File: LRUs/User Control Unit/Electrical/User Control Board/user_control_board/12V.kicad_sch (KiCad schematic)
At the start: 7 parts, among them U17 AMS1117-3.3

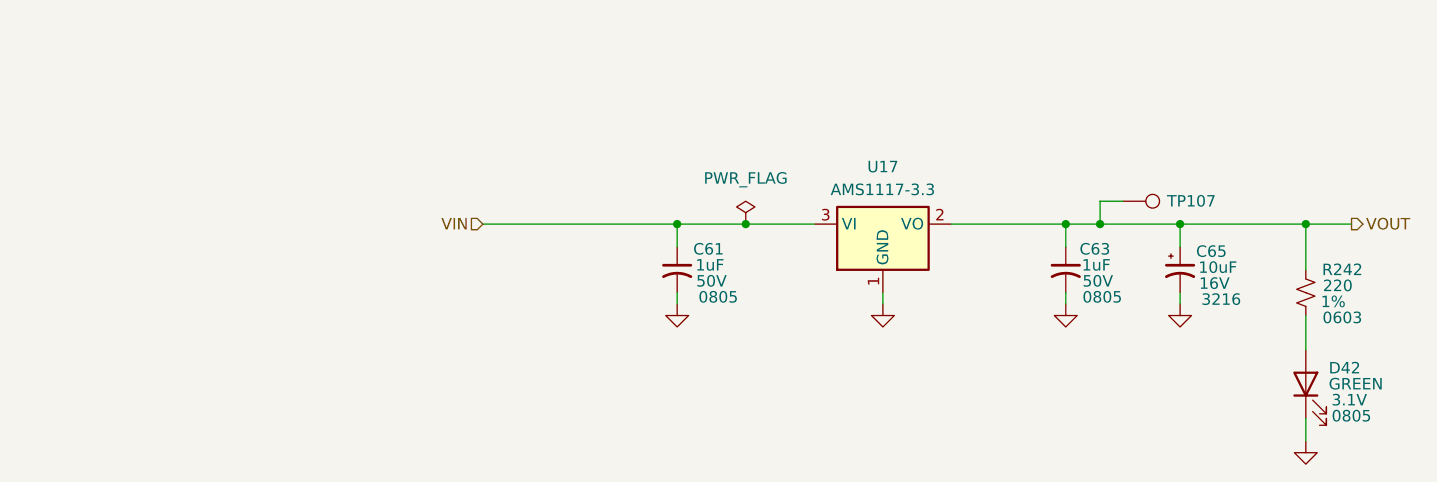
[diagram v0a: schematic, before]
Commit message: Added 12V XL6009 boost converter schematic
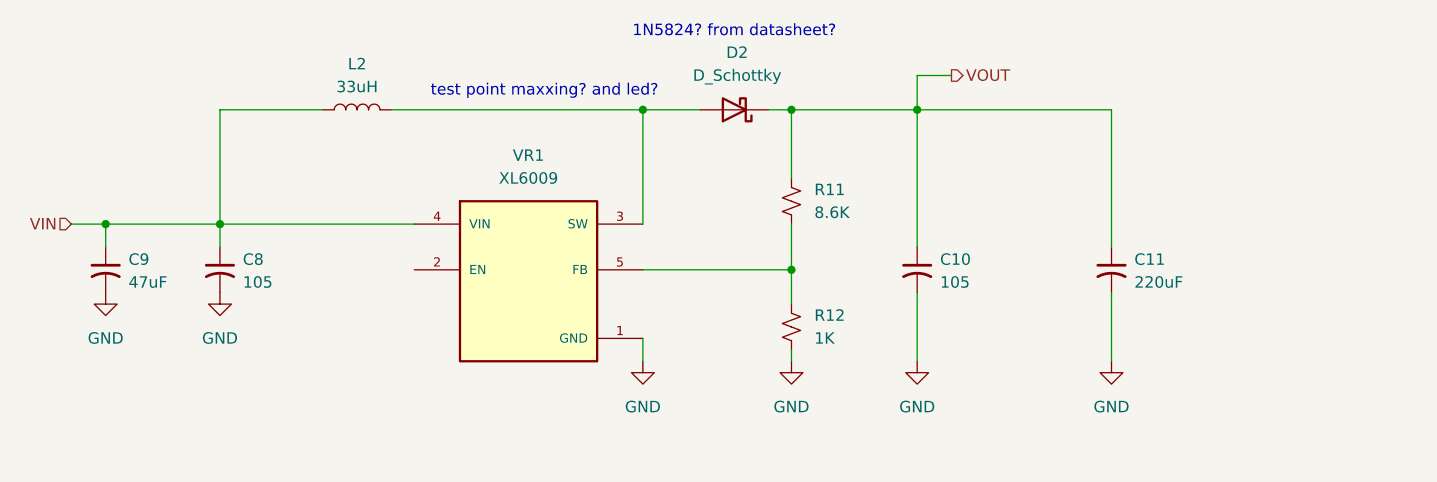
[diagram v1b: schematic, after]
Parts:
- removed C61, C63: 1uF, valve_pcb_footprints:C_0805_2012Metric, symbol Device:C_Small_US
- removed C65: 10uF, Capacitor_Tantalum_SMD:CP_EIA-3216-18_Kemet-A, symbol Device:C_Polarized_Small_US
- removed D42: GREEN, LED_SMD:LED_0805_2012Metric, symbol Device:LED
- removed R242: 220, valve_pcb_footprints:R_0603_1608Metric, symbol Device:R_Small_US
- removed TP107: TestPoint, TestPoint:TestPoint_Pad_D1.0mm, symbol Connector:TestPoint
- removed U17: AMS1117-3.3, Package_TO_SOT_SMD:SOT-223-3_TabPin2, symbol Regulator_Linear:AMS1117-3.3
- added C10: 105, Package_SO:SOIC-8_3.9x4.9mm_P1.27mm, symbol Device:C_Small_US
- added C11: 220uF, Package_SO:SOIC-8_3.9x4.9mm_P1.27mm, symbol Device:C_Small_US
- added C8: 105, XL6009:DPAK170P1435X465-6N, symbol Device:C_Small_US
- added C9: 47uF, symbol Device:C_Small_US
- added D2: D_Schottky, Diode_THT:D_DO-201AD_P15.24mm_Horizontal, symbol Device:D_Schottky
- added L2: 33uH, Relay_THT:Relay_DPDT_Finder_30.22, symbol Device:L
- added R11: 8.6K, symbol Device:R_Small_US
- added R12: 1K, symbol Device:R_Small_US
- added VR1: XL6009, XL6009:DPAK170P1435X465-6N, symbol XL6009:XL6009
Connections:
- net GND: now also C10.2, C11.2, C8.2, C9.2, R12.2, VR1.1 (GND)
- net VIN: now also C8.1, C9.1, L2.1, VR1.4 (VIN)
- net VOUT: now also C10.1, C11.1, D2.1 (K), R11.1
- new net: D2.2 (A), L2.2, VR1.3 (SW), VR1.6 (SW)
- new net: R11.2, R12.1, VR1.5 (FB)
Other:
- note added: "1N5824? from datasheet?"
- note added: "test point maxxing? and led?"

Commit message: footprint and added symbol for audio
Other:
- note added: "COILCRAFT FOR INDUCTOR"
- note added: "texus insturements 12 v boost regulator make schematic from input from 2s battery sends it to another connector *another screw terminal and that connector would send to external module xl6009."
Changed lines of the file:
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@@
+		)
+	)
+	(text "texus insturements 12 v boost regulator\n\nmake schematic from input from 2s battery sends it to another connector *another screw terminal and that connector would send to external module xl6009. "
+		(exclude_from_sim no)
+		(at 108.966 124.714 0)
+		(effects
+			(font
+				(size 1.27 1.27)
+			)
 		)
 	)
@@
 		(effects
 			(font
+				(size 1.27 1.27)
+			)
+		)
+	)
+	(text "COILCRAFT FOR INDUCTOR\n"
+		(exclude_from_sim no)
+		(at 85.852 61.722 0)
+		(effects
+			(font

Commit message: drc run
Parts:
- removed D2: D_Schottky, Diode_THT:D_DO-201AD_P15.24mm_Horizontal, symbol Device:D_Schottky
- removed VR1: XL6009, XL6009:DPAK170P1435X465-6N, symbol XL6009:XL6009
- added C12: 4.7uF, Package_LGA:Bosch_LGA-14_3x2.5mm_P0.5mm, symbol Device:C_Small_US
- added C13: 30pF, Package_LGA:Bosch_LGA-14_3x2.5mm_P0.5mm, symbol Device:C_Small_US
- added C14: 680pF, Package_LGA:Bosch_LGA-14_3x2.5mm_P0.5mm, symbol Device:C_Small_US
- added R10: 1.05M, Package_LGA:Bosch_LGA-14_3x2.5mm_P0.5mm, symbol Device:R_Small_US
- added R13: 32.4k, Package_LGA:Bosch_LGA-14_3x2.5mm_P0.5mm, symbol Device:R_Small_US
- added R14: 127k, Package_LGA:Bosch_LGA-14_3x2.5mm_P0.5mm, symbol Device:R_Small_US
- added TP10, TP6, TP7, TP8, TP9: TestPoint, symbol Connector:TestPoint
- added U1: TPS61089RNRR, RNR0011A, symbol symbols:TPS61089RNRR
- C10: value 105 -> 47uF; footprint Package_SO:SOIC-8_3.9x4.9mm_P1.27mm -> Package_LGA:Bosch_LGA-14_3x2.5mm_P0.5mm
- C11: value 220uF -> 100nF; footprint Package_SO:SOIC-8_3.9x4.9mm_P1.27mm -> Package_LGA:Bosch_LGA-14_3x2.5mm_P0.5mm
- C8: value 105 -> 10uF; footprint XL6009:DPAK170P1435X465-6N -> Package_LGA:Bosch_LGA-14_3x2.5mm_P0.5mm
- C9: value 47uF -> 100nF; footprint (none) -> Package_LGA:Bosch_LGA-14_3x2.5mm_P0.5mm
- L2: value 33uH -> 1.2uH; footprint Relay_THT:Relay_DPDT_Finder_30.22 -> (none)
- R11: value 8.6K -> 118k; footprint (none) -> Package_LGA:Bosch_LGA-14_3x2.5mm_P0.5mm
- R12: value 1K -> 309k; footprint (none) -> Package_LGA:Bosch_LGA-14_3x2.5mm_P0.5mm
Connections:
- net GND: now also R11.2, C12.2, C13.2, C14.2, R14.2, TP10.1, U1.5 (GND); no longer C9.2, R12.2
- net VIN: now also C10.1, C11.1, TP7.1, U1.9 (VIN); no longer C8.1, C9.1
- net VOUT: now also C8.1, R10.1, TP6.1, U1.6 (VOUT); no longer C10.1, C11.1, R11.1
- net at L2.2: now also C9.2, R12.1, TP8.1, U1.11 (SW)
- new net: R12.2, U1.1 (FSW)
- new net: C9.1, U1.10 (BOOT)
- new net: C12.1, U1.2 (VCC), U1.7 (EN)
- new net: R10.2, R11.1, TP9.1, U1.3 (FB)
- new net: C13.1, R13.1, U1.4 (COMP)
- new net: R14.1, U1.8 (ILIM)
- new net: C14.1, R13.2
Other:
- note removed: "1N5824? from datasheet?"
- note removed: "test point maxxing? and led?"
- note removed: "texus insturements 12 v boost regulator make schematic from input from 2s battery sends it to another connector *another screw terminal and that connector would send to external module xl6009."

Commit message: need to run DCR
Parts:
- removed R11: 118k, Package_LGA:Bosch_LGA-14_3x2.5mm_P0.5mm, symbol Device:R_Small_US
- added R16: 18k, valve_pcb_footprints:R_0603_1608Metric, symbol Device:R_Small_US
- added R17: 100k, valve_pcb_footprints:R_0603_1608Metric, symbol Device:R_Small_US
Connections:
- net GND: now also R16.2
- net at R10.2, TP9.1, U1.3 (FB): now also R17.1
- new net: R16.1, R17.2
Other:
- note added: "ILIM = 1030000/RILIM = 8 A"
- note added: "Target FSW = 1.2MHz"
- note added: "Used TI power designer for this."
- note added: "VFB = VOUT * RBOT/(RTOP + RBOT) VOUT = 1.212 (1+ (RTOP/BOT)) VOUT = 1.212 (1+ (1.05*10^6/118*10^3)) = 12"
- note added: "VIN = 7.4 NOMINAL"
- note removed: "COILCRAFT FOR INDUCTOR"
- moved on the sheet: R14, TP10

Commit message: connectors and 5v buck partially done
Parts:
- removed C10: 47uF, Package_LGA:Bosch_LGA-14_3x2.5mm_P0.5mm, symbol Device:C_Small_US
- removed C11, C9: 100nF, Package_LGA:Bosch_LGA-14_3x2.5mm_P0.5mm, symbol Device:C_Small_US
- removed C12: 4.7uF, Package_LGA:Bosch_LGA-14_3x2.5mm_P0.5mm, symbol Device:C_Small_US
- removed C8: 10uF, Package_LGA:Bosch_LGA-14_3x2.5mm_P0.5mm, symbol Device:C_Small_US
- removed R10: 1.05M, Package_LGA:Bosch_LGA-14_3x2.5mm_P0.5mm, symbol Device:R_Small_US
- removed R12: 309k, Package_LGA:Bosch_LGA-14_3x2.5mm_P0.5mm, symbol Device:R_Small_US
- removed R13: 32.4k, Package_LGA:Bosch_LGA-14_3x2.5mm_P0.5mm, symbol Device:R_Small_US
- removed R14: 127k, Package_LGA:Bosch_LGA-14_3x2.5mm_P0.5mm, symbol Device:R_Small_US
- removed U1: TPS61089RNRR, RNR0011A, symbol symbols:TPS61089RNRR
- added C15: 47uF, Capacitor_SMD:C_1206_3216Metric, symbol Device:C_Small_US
- added C16, C20: 100nF, Capacitor_SMD:C_0402_1005Metric, symbol Device:C_Small_US
- added C17: 4.7uF, Capacitor_SMD:C_0805_2012Metric, symbol Device:C_Small_US
- added C18: 30pF, Capacitor_SMD:C_0201_0603Metric, symbol Device:C_Small_US
- added C19: 680pF, Capacitor_SMD:C_0201_0603Metric, symbol Device:C_Small_US
- added C21, C22, C23: 10uF, Capacitor_Tantalum_SMD:CP_EIA-7343-31_Kemet-D, symbol Device:C_Polarized_Small_US
- added R19: 32.4k, Resistor_SMD:R_0603_1608Metric, symbol Device:R_Small_US
- added R20: 127k, Resistor_SMD:R_0603_1608Metric, symbol Device:R_Small_US
- added R21: 309k, Resistor_SMD:R_0603_1608Metric, symbol Device:R_Small_US
- added R22: 1.05M, Resistor_SMD:R_0603_1608Metric, symbol Device:R_Small_US
- added U4: TPS61089RNRR, Package_DFN_QFN:Texas_VQFN-RNR0011A-11, symbol symbols:TPS61089RNRR
- C13: value 30pF -> 47uF; footprint Package_LGA:Bosch_LGA-14_3x2.5mm_P0.5mm -> Capacitor_SMD:C_1206_3216Metric; Footprint_Size (none) -> 1206; JLCPCB Part # (none) -> C76659; Vmax (none) -> 25v
- C14: value 680pF -> 47uF; footprint Package_LGA:Bosch_LGA-14_3x2.5mm_P0.5mm -> Capacitor_SMD:C_1206_3216Metric; Footprint_Size (none) -> 1206; JLCPCB Part # (none) -> C76659; Vmax (none) -> 25v
- L2: footprint (none) -> Inductor_SMD:L_Coilcraft_XAL6030-XXX; Footprint_Size (none) -> XAL6030; IMAX (none) -> 12A; JLCPCB Part # (none) -> C19191689
- R23: renamed from R17; footprint valve_pcb_footprints:R_0603_1608Metric -> Resistor_SMD:R_0603_1608Metric
- R24: renamed from R16; footprint valve_pcb_footprints:R_0603_1608Metric -> Resistor_SMD:R_0603_1608Metric
- TP10: renamed from TP9; footprint (none) -> TestPoint:TestPoint_Pad_D1.0mm
- TP11: renamed from TP10; footprint (none) -> TestPoint:TestPoint_Pad_D1.0mm
- TP12: renamed from TP6; footprint (none) -> TestPoint:TestPoint_Pad_D1.0mm
- TP8: renamed from TP7; footprint (none) -> TestPoint:TestPoint_Pad_D1.0mm
- TP9: renamed from TP8; footprint (none) -> TestPoint:TestPoint_Pad_D1.0mm
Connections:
- net GND: now also C15.2, C16.2, C17.2, C18.2, C19.2, C21.2, C22.2, C23.2, R20.1, U4.5 (GND)
- net VIN: now also C13.1, C14.1, C15.1, C16.1, U4.9 (VIN)
- net VOUT: now also C21.1, C22.1, C23.1, R22.1, U4.6 (VOUT)
- net at L2.2, TP9.1: now also C20.2, R21.2, U4.11 (SW)
- net at R23.1, TP10.1: now also R22.2, U4.3 (FB)
- new net: R20.2, U4.8 (ILIM)
- new net: C19.1, R19.1
- new net: C18.1, R19.2, U4.4 (COMP)
- new net: R21.1, U4.1 (FSW)
- new net: C17.1, U4.2 (VCC), U4.7 (EN)
- new net: C20.1, U4.10 (BOOT)
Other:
- note added: "0402, 3216, 7342, 0805 cap size"
- note added: "C19191689"
- moved on the sheet: R23, R24, TP10, TP11, TP12, TP8, TP9

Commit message: 12V partially done. need to add 3d model
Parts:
- removed TP9: TestPoint, TestPoint:TestPoint_Pad_D1.0mm, symbol Connector:TestPoint
